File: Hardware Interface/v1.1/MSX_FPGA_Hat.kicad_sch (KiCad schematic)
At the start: 24 parts, among them J1 J1, J2 J2, J3a1 J3a, J3b1 J3b, J4a1 J4a, J4b1 J4b, U1 74LVC245A, U2 74LVC245A, U3 74LVC245A, U4 74LVC245A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

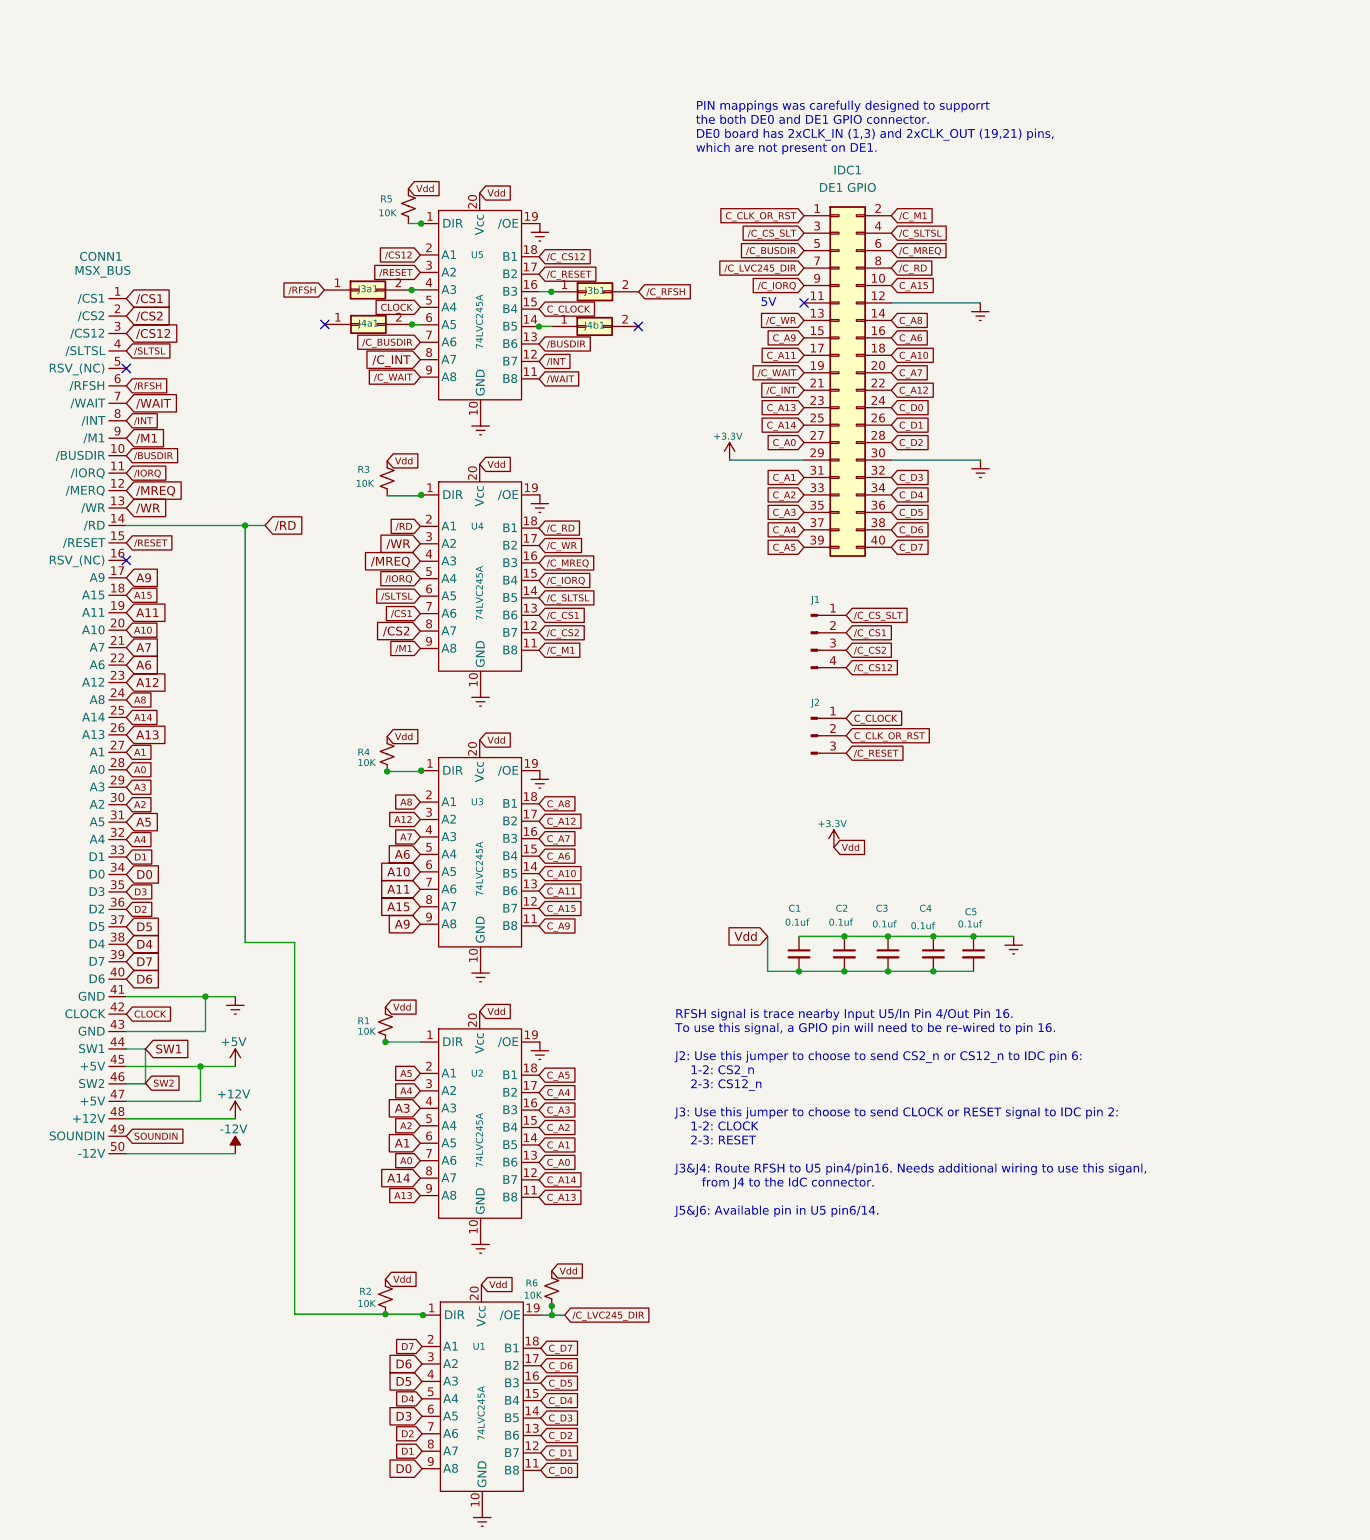
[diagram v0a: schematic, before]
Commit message: Moving to version 1.2 as it's clear that the OD pin in the U1 is not being driven correctly and need a separate pin for this purpose. V1.2 has this change implemented
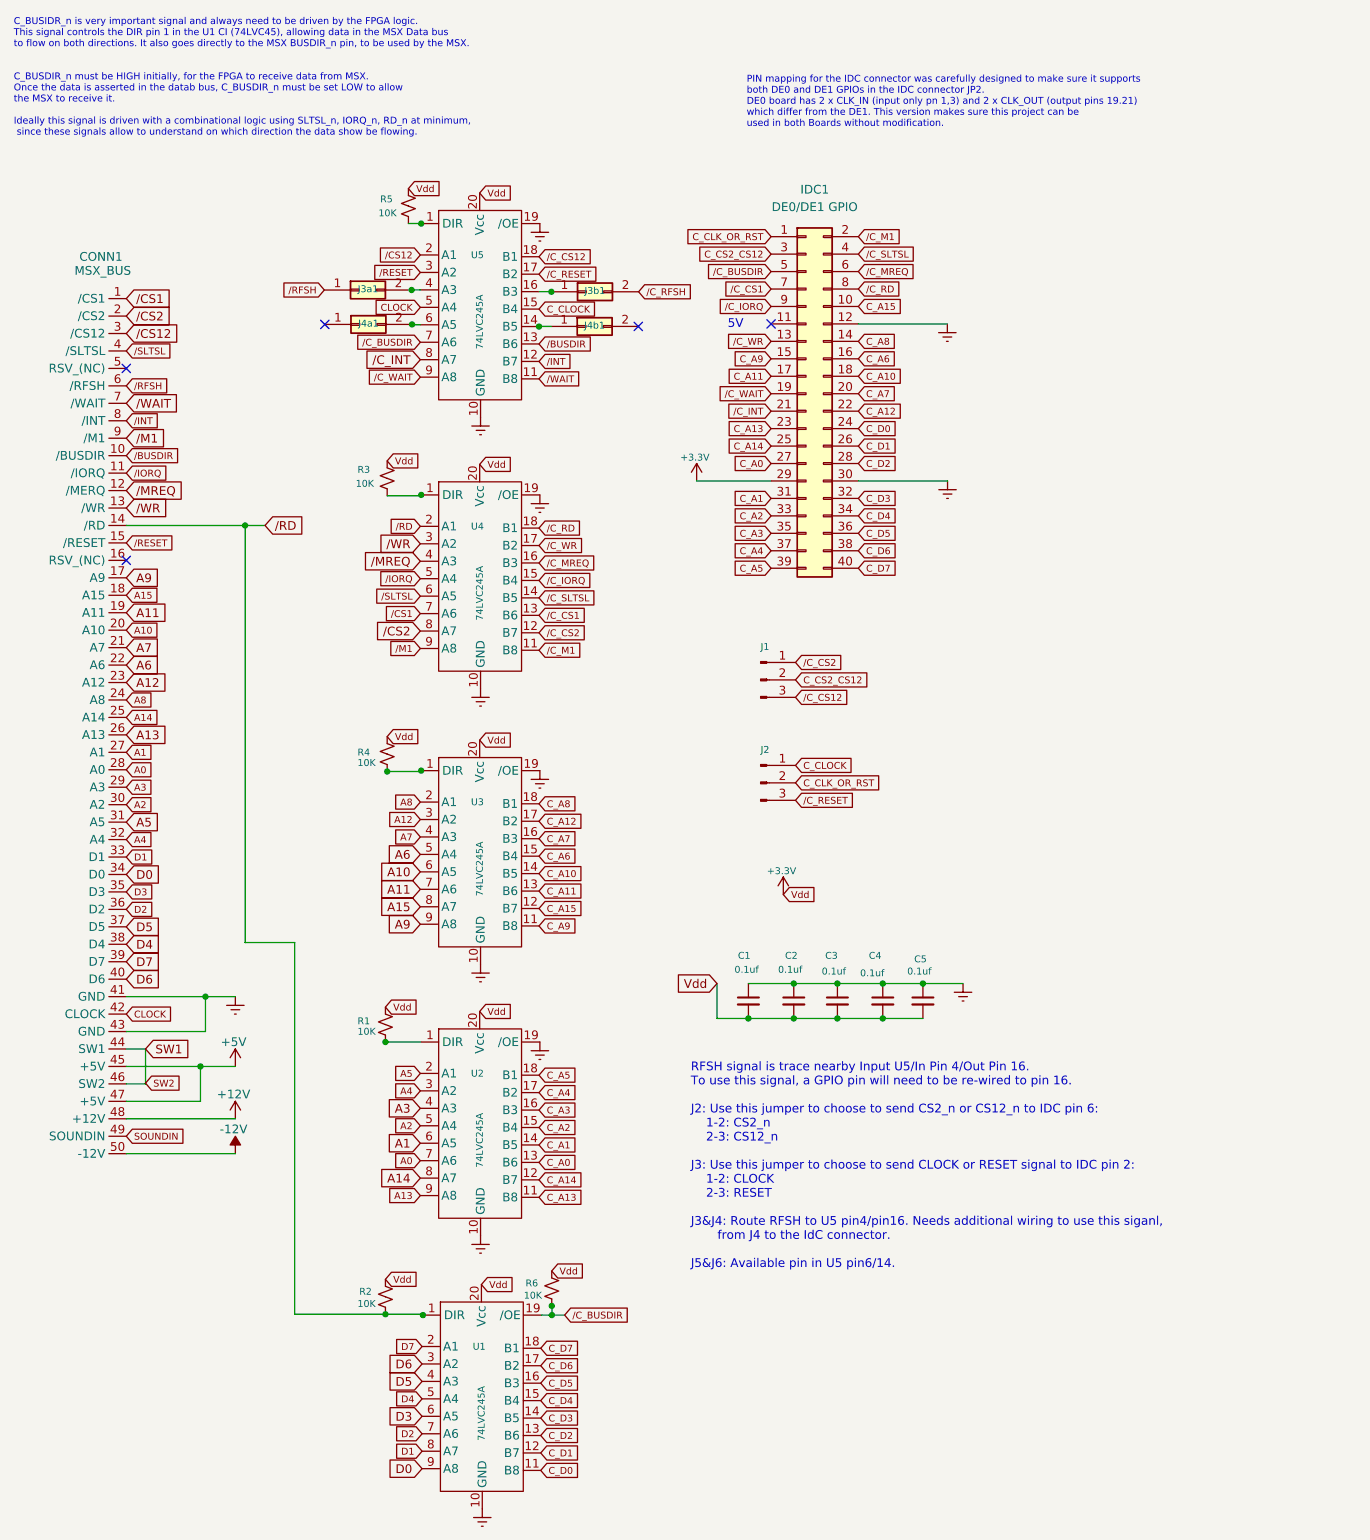
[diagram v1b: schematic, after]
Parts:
- IDC1: value DE1 GPIO -> DE0/DE1 GPIO
- J1: footprint Connector_PinHeader_2.54mm:PinHeader_2x02_P2.54mm_Vertical -> Connector_PinHeader_2.54mm:PinHeader_1x03_P2.54mm_Vertical; symbol Connector:Conn_01x04_Male -> Connector:Conn_01x03_Male
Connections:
- net /C_BUSDIR: now also R6.2, U1.19 (/OE)
- net /C_CS1: now also IDC1.7 (Pin_7); no longer J1.2 (Pin_2)
- net /C_CS12: now also J1.3 (Pin_3); no longer J1.4 (Pin_4)
- net /C_CS2: now also J1.1 (Pin_1); no longer J1.3 (Pin_3)
- net /C_CS_SLT renamed C_CS2_CS12
- net C_CS2_CS12: now also J1.2 (Pin_2); no longer J1.1 (Pin_1)
- removed net /C_LVC245_DIR: IDC1.7 (Pin_7), R6.2, U1.19 (/OE)
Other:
- note added: "C_BUSIDR_n is very important signal and always need to be driven by the FPGA logic. This signal controls the DIR pin 1 in the U1 CI (74LVC45), allowing data in the MSX Data bus to flow on both directions. It also goes directly to the MSX BUSDIR_n pin, to be used by the MSX. C_BUSDIR_n must be HIGH initially, for the FPGA to receive data from MSX. Once the data is asserted in the datab bus, C_BUSD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"
- note added: "PIN mapping for the IDC connector was carefully designed to make sure it supports both DE0 and DE1 GPIOs in the IDC connector JP2. DE0 board has 2 x CLK_IN (input only pn 1,3) and 2 x CLK_OUT (output pins 19.21) which differ from the DE1. This version makes sure this project can be used in both Boards without modification."
- note removed: "PIN mappings was carefully designed to supporrt the both DE0 and DE1 GPIO connector. DE0 board has 2xCLK_IN (1,3) and 2xCLK_OUT (19,21) pins, which are not present on DE1."
- moved on the sheet: C1, C2, C3, C4, C5, IDC1, J2
